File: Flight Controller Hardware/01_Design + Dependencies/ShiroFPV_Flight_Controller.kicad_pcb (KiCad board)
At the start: 4 copper layers, 40 x 40 mm, 117 parts, among them J1 GND, J10 TLM, J11 Video_Out, J12 Video_IN, J13 5V3, J14 RX3, J15 TX3, J16 GND3, J17 5V4, J18 RX4, J19 TX4, J2 GND, J20 GND4, J24 +5V, J25 RSSI, J26 GND5, J29 SBUS, J3 VBAT, J30 5V5, J31 RX5, J32 TX5, J33 RX6, J34 5V6, J35 GND6, J36 TX6, J37 10V, J38 RX1, J39 TX1, J4 VBAT, J40 GND1, J42 B-, J46 GND, J5 M1, J6 M2, J7 M3, J8 M4, J9 CUR, P1 USB_C_Plug_USB2.0, Q1 AO3401A, Q2 AO3400A, Q3 BC817W, U1 AT32F435RGT7, U10 AT7456, U3 ICM-20602, U4 BME280, U5 TPS54302, U6 TPS54302DDCR, U7 RT9013-33GB, U8 W25Q128JVS, Y2 27MHz

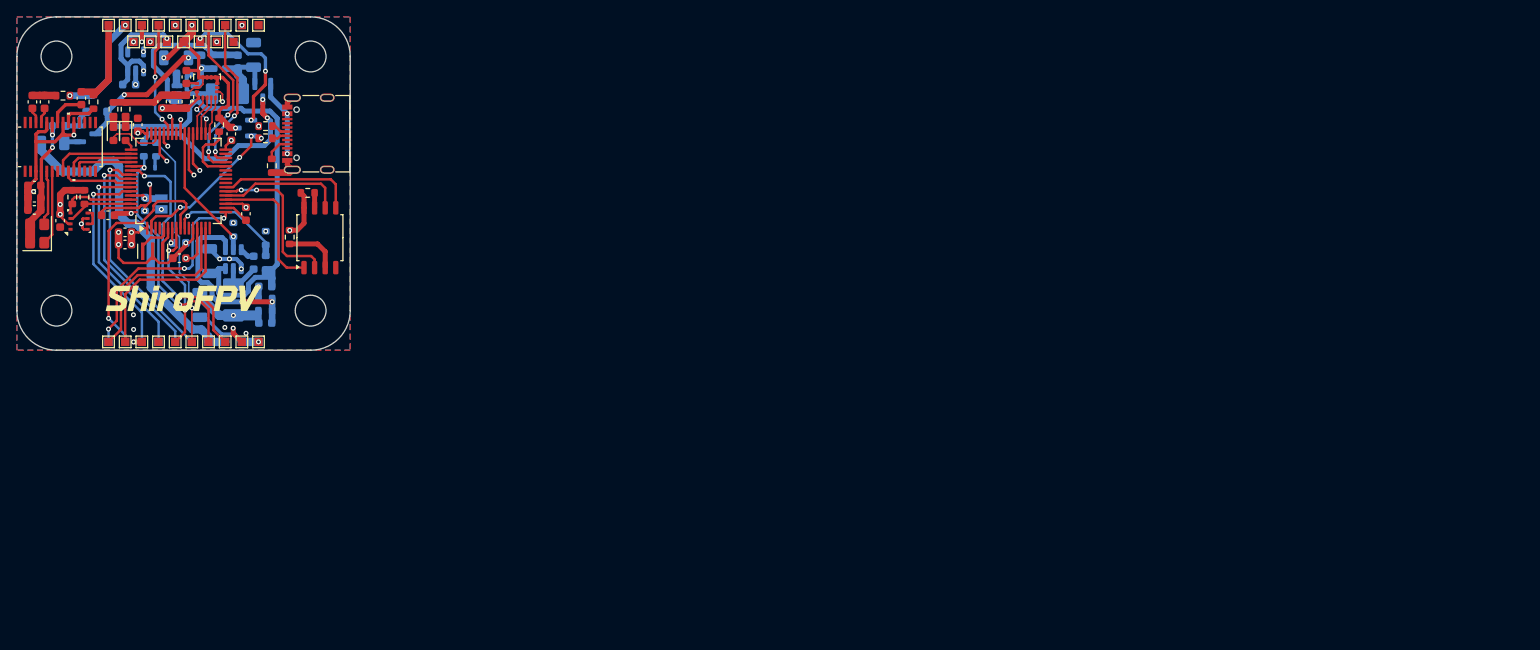
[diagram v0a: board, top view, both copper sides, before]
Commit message: Fixed Mistake
Fixed a mistake made in the Pin Config of two Mosfets.
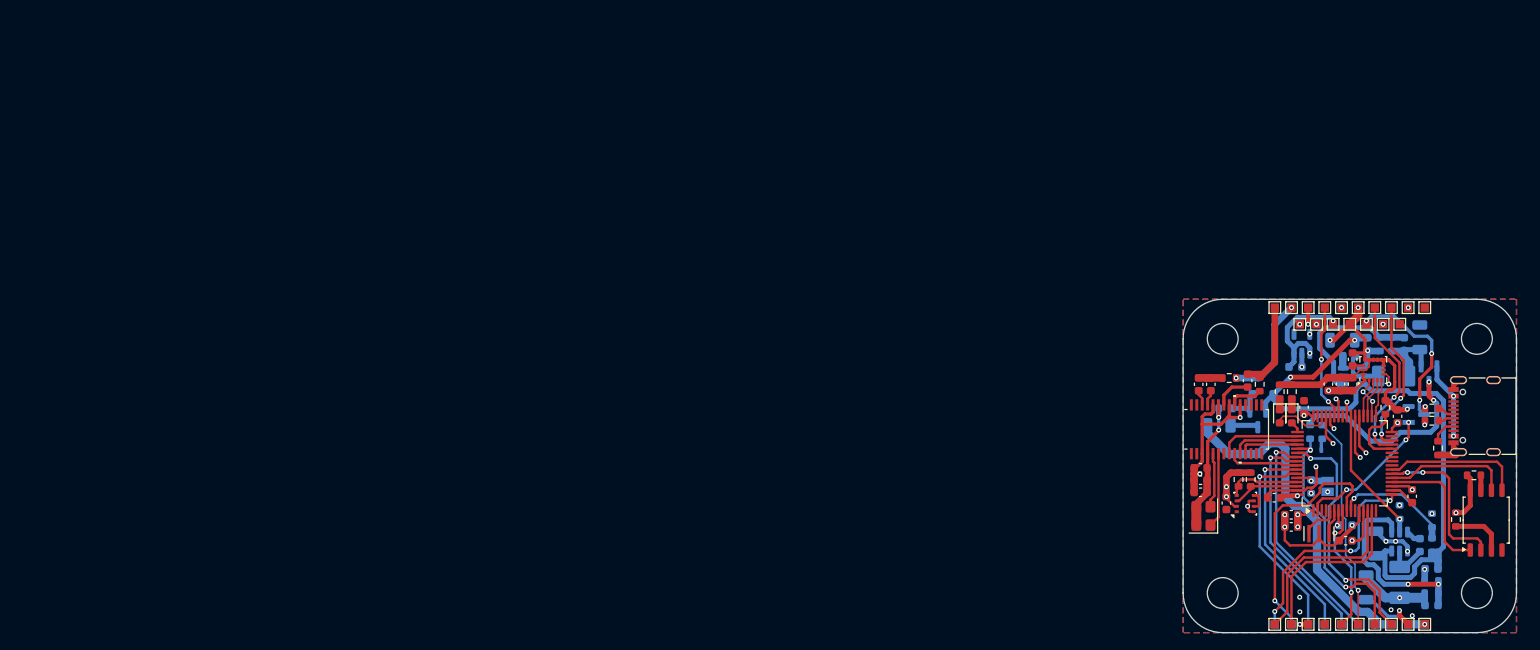
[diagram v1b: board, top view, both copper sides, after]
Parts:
- removed G***: LOGO, LOGO
- moved Q2 145.3 mm to (210.2, 84.3)
- moved Q1 144.6 mm to (190.8, 85.3), turned to 90 degrees
- moved C10 144.0 mm to (187.0, 95.0)
- moved C11 144.0 mm to (189.6, 80.3)
- moved C12 144.0 mm to (183.9, 92.2)
- moved C13 144.0 mm to (183.9, 90.8)
- moved C14 144.0 mm to (205.0, 99.8)
- moved C15 144.0 mm to (204.0, 75.9)
- moved C16 144.0 mm to (210.2, 100.0)
- moved C17 144.0 mm to (208.3, 75.9)
- moved C18 144.0 mm to (210.2, 75.1)
- moved C19 144.0 mm to (203.8, 105.1)
- moved C2 144.0 mm to (201.8, 77.3)
- moved C20 144.0 mm to (211.6, 102.9)
- moved C22 144.0 mm to (211.6, 107.2)
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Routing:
- net Net-(Q1-D): track 1.94 -> 3.56 mm
- net GND: track 118.7 -> 120.2 mm
- net BEEPER_B-: track 17.9 -> 19.4 mm
- net BEEPER: track 17.8 -> 16.9 mm
- net Net-(D1-A): track 3.67 -> 4.48 mm
- net USBD+: track 17.4 -> 17.9 mm
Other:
- outline, holes or cut-outs redrawn

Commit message: Lots of new stuff
Added a new Website thus it not beeing finished yet.
and updated the PCB
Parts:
- added G***: LOGO, LOGO, F.Cu at (202.2, 75.5)
- J1, J10, J11, J12, J13, J14, J15, J16, J17, J18, J19, J2, J20, J24, J25, J26, J29, J3, J30, J31, J32, J33, J34, J35, J36, J37, J38, J39, J4, J40, J42, J46, J5, J6, J7, J8, J9: footprint TestPoint:TestPoint_Pad_1.0x1.0mm -> TestPoint:TestPoint_Pad_1.0x1.0mm_No_Silkscreen
- moved REF** 43.4 mm to (217.4, 75.3), turned to 90 degrees
- moved REF** 43.4 mm to (217.4, 105.8), turned to 90 degrees
- moved REF** 42.9 mm to (186.9, 105.8), turned to 90 degrees
- moved REF** 42.9 mm to (186.9, 75.3), turned to 90 degrees
- moved J10 42.2 mm to (211.2, 71.5), turned to -90 degrees
- moved J19 42.2 mm to (211.2, 71.5), turned to 90 degrees
- moved J12 42.2 mm to (211.2, 109.5), turned to 90 degrees
- moved J46 41.9 mm to (193.2, 109.5), turned to 90 degrees
- moved J1 41.9 mm to (193.2, 71.5), turned to -90 degrees
- moved J40 41.9 mm to (193.2, 71.5), turned to 90 degrees
- moved C8 41.5 mm to (220.3, 100.3), turned to -90 degrees
- moved J18 40.6 mm to (209.2, 71.5), turned to 90 degrees
- moved J9 40.6 mm to (209.2, 71.5), turned to -90 degrees
- moved J11 40.6 mm to (209.2, 109.5), turned to 90 degrees
- moved J17 40.4 mm to (195.2, 71.5), turned to 90 degrees
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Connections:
- Y2 pad 3: (no net) -> GND
- Y2 pad 4: (no net) -> GND
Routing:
- net +3.3V: track 37.5 -> 45.5 mm, vias 15 -> 13
- net +5V: track 62.4 -> 66.8 mm
- net GND: track 120.2 -> 123.3 mm, vias 22 -> 20
- net Net-(U5-FB): track 18.6 -> 15.6 mm
- net VBUS: track 9.20 -> 11.0 mm, vias 2 -> 1
- net USBD+: track 17.9 -> 16.5 mm
- net VBAT: track 40.8 -> 39.4 mm
- net BEEPER: track 16.9 -> 18.2 mm
- net BEEPER_B-: track 19.4 -> 20.4 mm
- net BOOT0: track 3.88 -> 4.83 mm
- net ADC_CURRENT: track 28.6 -> 29.5 mm
- net +10V: track 47.3 -> 48.1 mm, vias 2 -> 4
- net V_IN: track 11.6 -> 10.7 mm
- net SBUS: track 25.7 -> 26.4 mm
- net UART5RX: track 29.6 -> 30.2 mm
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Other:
- outline, holes or cut-outs redrawn
- board text added: "Front"
- board text added: "R13"
